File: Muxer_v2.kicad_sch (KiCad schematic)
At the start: 5 parts, among them J1 Conn_01x06_Pin

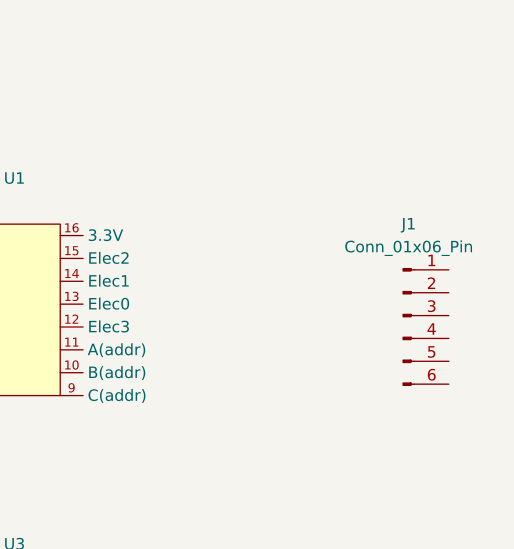
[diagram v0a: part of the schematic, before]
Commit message: Remade 6-pin connector footprint, added it to schematic file
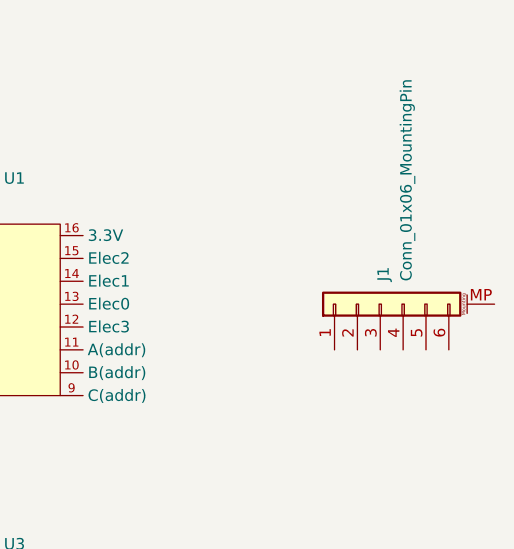
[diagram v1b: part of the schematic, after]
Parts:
- removed J1: Conn_01x06_Pin, symbol Connector:Conn_01x06_Pin
- added J1: Conn_01x06_MountingPin, Connector_6_pin:6_pin_ocusound, symbol Connector_Generic_MountingPin:Conn_01x06_MountingPin
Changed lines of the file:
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@@
-	)
-	(symbol
-		(lib_id "Connector:Conn_01x06_Pin")
-		(at 144.78 73.66 0)
-		(unit 1)
-		(exclude_from_sim no)
-		(in_bom yes)
-		(on_board yes)
-		(dnp no)
-		(fields_autoplaced yes)
-		(property "Reference" "J1"
-			(at 145.415 63.5 0)
-			(effects
-				(font
-					(size 1.27 1.27)
-				)
-			)
-		)
-		(property "Value" "Conn_01x06_Pin"
-			(at 145.415 66.04 0)
-			(effects
-				(font
-					(size 1.27 1.27)
-				)
-			)
-		)
-		(property "Footprint" ""
-			(at 144.78 73.66 0)
-			(effects
-				(font
-					(size 1.27 1.27)
-				)
-				(hide yes)
-			)
-		)
-		(property "Datasheet" "~"
-			(at 144.78 73.66 0)
-			(effects
-				(font
-					(size 1.27 1.27)
-				)
-				(hide yes)
-			)
-		)
-		(property "Description" "Generic connector, single row, 01x06, script generated"
-			(at 144.78 73.66 0)
-			(effects
-				(font
-					(size 1.27 1.27)
-				)
-				(hide yes)
-			)
-		)
-		(pin "4"
-		)
-		(pin "5"
-		)
-		(pin "6"
-		)
-		(pin "3"
-		)
-		(pin "2"
-		)
-		(pin "1"
-		)
-		(instances
-			(project ""
-				(path "/dce75761-2727-441f-b46b-c25c179f2eb7"
-					(reference "J1")
-					(unit 1)
-				)
-			)
-		)
 	)
 	(symbol
@@
 					(unit 1)
 				)
+			)
+		)
+	)
+	(symbol
+		(lib_id "Connector_Generic_MountingPin:Conn_01x06_MountingPin")
+		(at 142.24 72.39 90)
+		(unit 1)
+		(exclude_from_sim no)
+		(in_bom yes)
+		(on_board yes)
+		(dnp no)
+		(property "Reference" "J1"
+			(at 142.5955 69.85 0)
+			(effects
+				(font
+					(size 1.27 1.27)
+				)
+				(justify left)
+			)
+		)
+		(property "Value" "Conn_01x06_MountingPin"
+			(at 145.1355 69.85 0)
+			(effects
+				(font
+					(size 1.27 1.27)
+				)
+				(justify left)
+			)
+		)
+		(property "Footprint" "Connector_6_pin:6_pin_ocusound"
+			(at 142.24 72.39 0)
+			(effects
+				(font
+					(size 1.27 1.27)
+				)
+				(hide yes)
+			)
+		)
+		(property "Datasheet" "~"
+			(at 142.24 72.39 0)
+			(effects
+				(font
+					(size 1.27 1.27)
+				)
+				(hide yes)
+			)
+		)
+		(property "Description" "Generic connectable mounting pin connector, single row, 01x06, script generated (kicad-library-utils/schlib/autogen/connector/)"
+			(at 142.24 72.39 0)
+			(effects
+				(font
+					(size 1.27 1.27)
+				)
+				(hide yes)
+			)
+		)
+		(pin "6"
+		)
+		(pin "5"
+		)
+		(pin "4"
+		)
+		(pin "3"
+		)
+		(pin "2"
+		)
+		(pin "1"
+		)
+		(pin "MP"
+		)
+		(instances
+			(project ""
+				(path "/dce75761-2727-441f-b46b-c25c179f2eb7"
+					(reference "J1")
+					(unit 1)
+				)

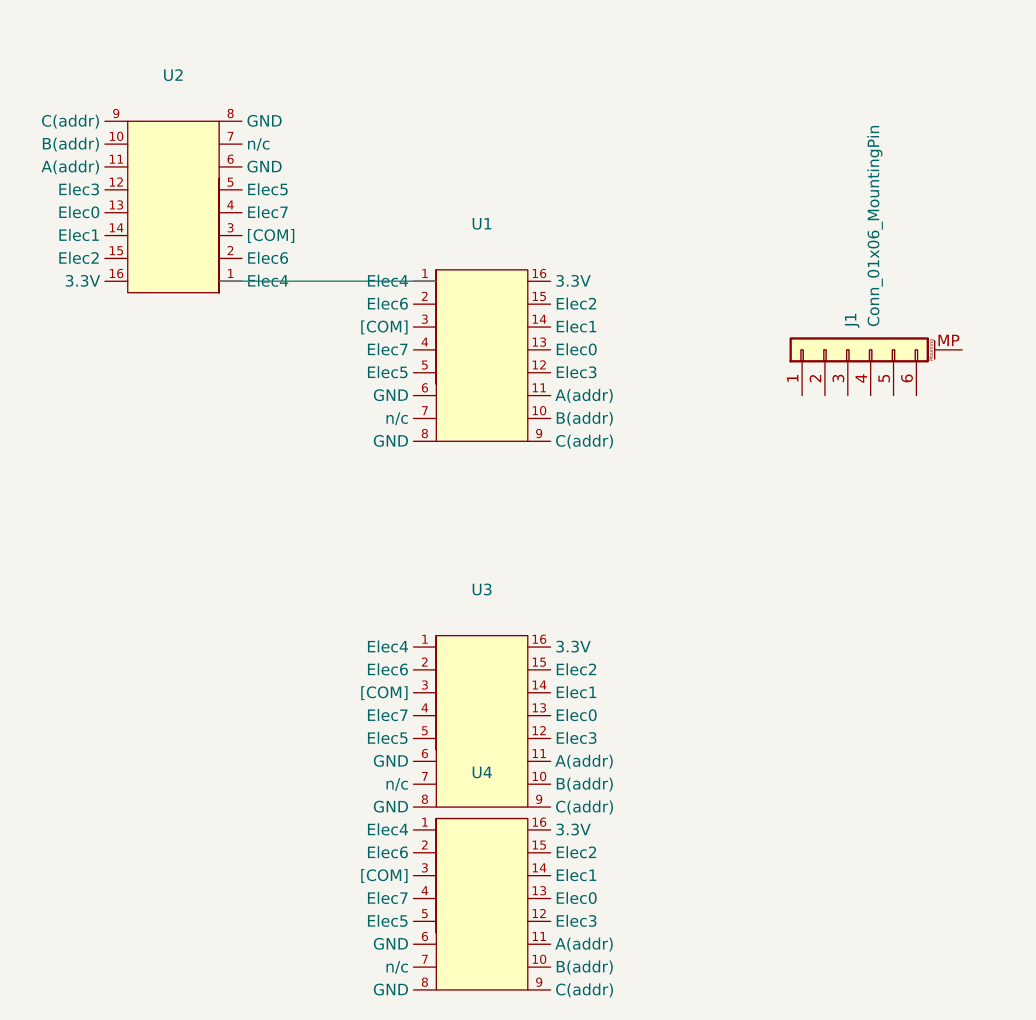
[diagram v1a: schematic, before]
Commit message: Started electrode wire connections, attached 6-pin connector to input areas
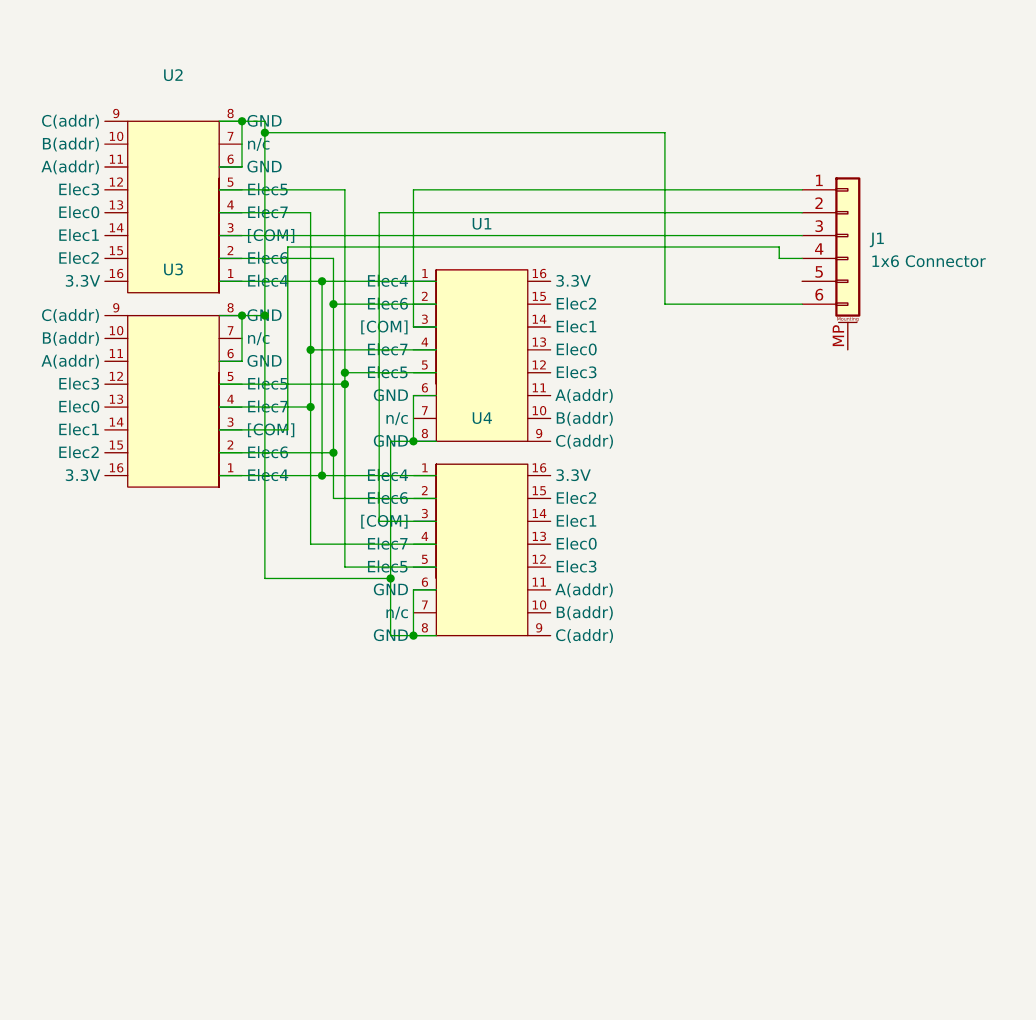
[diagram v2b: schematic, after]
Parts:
- J1: value Conn_01x06_MountingPin -> 1x6 Connector
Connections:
- net at U4.1 (Elec4): now also U1.1 (Elec4), U2.1 (Elec4), U3.1 (Elec4)
- net at U4.2 (Elec6): now also U1.2 (Elec6), U2.2 (Elec6), U3.2 (Elec6)
- net at U4.3 ([COM]): now also J1.2 (F-)
- net at U4.4 (Elec7): now also U1.4 (Elec7), U2.4 (Elec7), U3.4 (Elec7)
- net at U4.5 (Elec5): now also U1.5 (Elec5), U2.5 (Elec5), U3.5 (Elec5)
- net at U4.6 (GND): now also J1.6 (GND), U1.6 (GND), U1.8 (GND), U2.6 (GND), U2.8 (GND), U3.6 (GND), U3.8 (GND), U4.8 (GND)
- net at U1.3 ([COM]): now also J1.1 (F+)
- net at U3.3 ([COM]): now also J1.4 (S-)
- net at U2.3 ([COM]): now also J1.3 (S+)
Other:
- moved on the sheet: J1, U3, U4

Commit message: Configured multiplexer setup, added 8 and 3 pin connectors
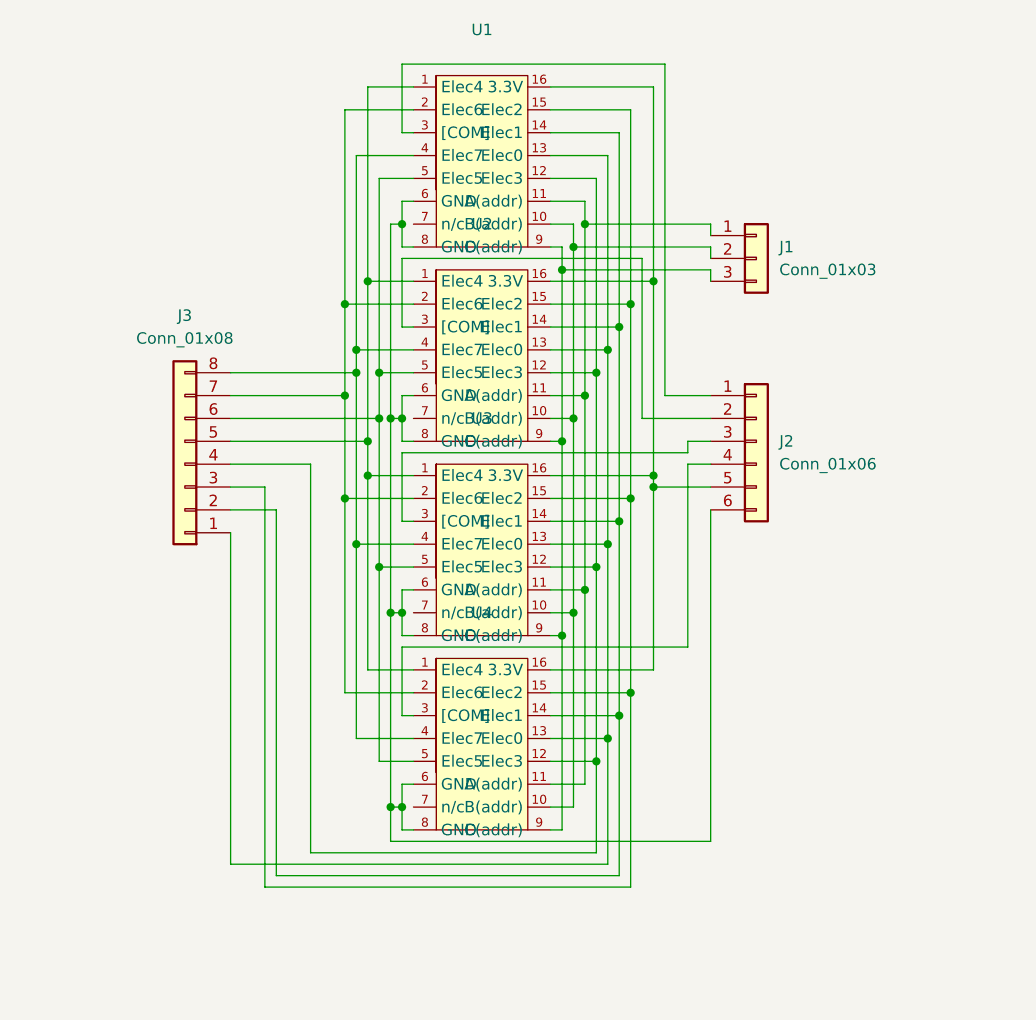
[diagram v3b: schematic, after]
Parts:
- removed J1: 1x6 Connector, Connector_6_pin:6_pin_ocusound, symbol Connector_Generic_MountingPin:Conn_01x06_MountingPin
- added J1: Conn_01x03, Connector_PinHeader_2.54mm:PinHeader_1x03_P2.54mm_Vertical, symbol Connector_Generic:Conn_01x03
- added J2: Conn_01x06, Connector_PinHeader_2.54mm:PinHeader_1x06_P2.54mm_Vertical, symbol Connector_Generic:Conn_01x06
- added J3: Conn_01x08, Connector_PinHeader_2.54mm:PinHeader_1x08_P2.54mm_Vertical, symbol Connector_Generic:Conn_01x08
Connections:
- net at U1.1 (Elec4), U2.1 (Elec4), U3.1 (Elec4)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: now also J3.5 (Pin_5)
- net at U4.10 (B(addr)): now also U1.10 (B(addr)), U2.10 (B(addr)), U3.10 (B(addr)), J1.2 (B)
- net at U4.11 (A(addr)): now also U1.11 (A(addr)), U2.11 (A(addr)), U3.11 (A(addr)), J1.1 (A)
- net at U4.12 (Elec3): now also U1.12 (Elec3), U2.12 (Elec3), U3.12 (Elec3), J3.4 (Pin_4)
- net at U4.13 (Elec0): now also U1.13 (Elec0), U2.13 (Elec0), U3.13 (Elec0), J3.1 (Pin_1)
- net at U4.14 (Elec1): now also U1.14 (Elec1), U2.14 (Elec1), U3.14 (Elec1), J3.2 (Pin_2)
- net at U4.15 (Elec2): now also U1.15 (Elec2), U2.15 (Elec2), U3.15 (Elec2), J3.3 (Pin_3)
- net at U4.16 (3.3V): now also U1.16 (3.3V), U2.16 (3.3V), U3.16 (3.3V), J2.5 (3.3_V)
- net at U1.2 (Elec6), U2.2 (Elec6), U3.2 (Elec6)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: now also J3.7 (Pin_7)
- net at U4.3 ([COM]): now also J2.4 (S-)
- net at U1.4 (Elec7), U2.4 (Elec7), U3.4 (Elec7)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: now also J3.8 (Pin_8)
- net at U1.5 (Elec5), U2.5 (Elec5), U3.5 (Elec5)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: now also J3.6 (Pin_6)
- net at U1.6 (GND), U1.8 (GND), U2.6 (GND)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: now also J2.6 (GND)
- net at U4.9 (C(addr)): now also U1.9 (C(addr)), U2.9 (C(addr)), U3.9 (C(addr)), J1.3 (C)
- net at U1.3 ([COM]): now also J2.1 (F+)
- net at U3.3 ([COM]): now also J2.3 (S+)
- net at U2.3 ([COM]): now also J2.2 (F-)
